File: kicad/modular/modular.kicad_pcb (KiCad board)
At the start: 2 copper layers, 119.1 x 78 mm, 84 parts, among them J1 CONN_PWR, J2 HEADER, J3 HEADER, J4 Header, J5 DIFFX, J6 DIFFY, J7 SUM, U1 LM317, U2 LM337, U3 REF5010, U4 OPA4197, U5 OPA197, U6 OPA2197

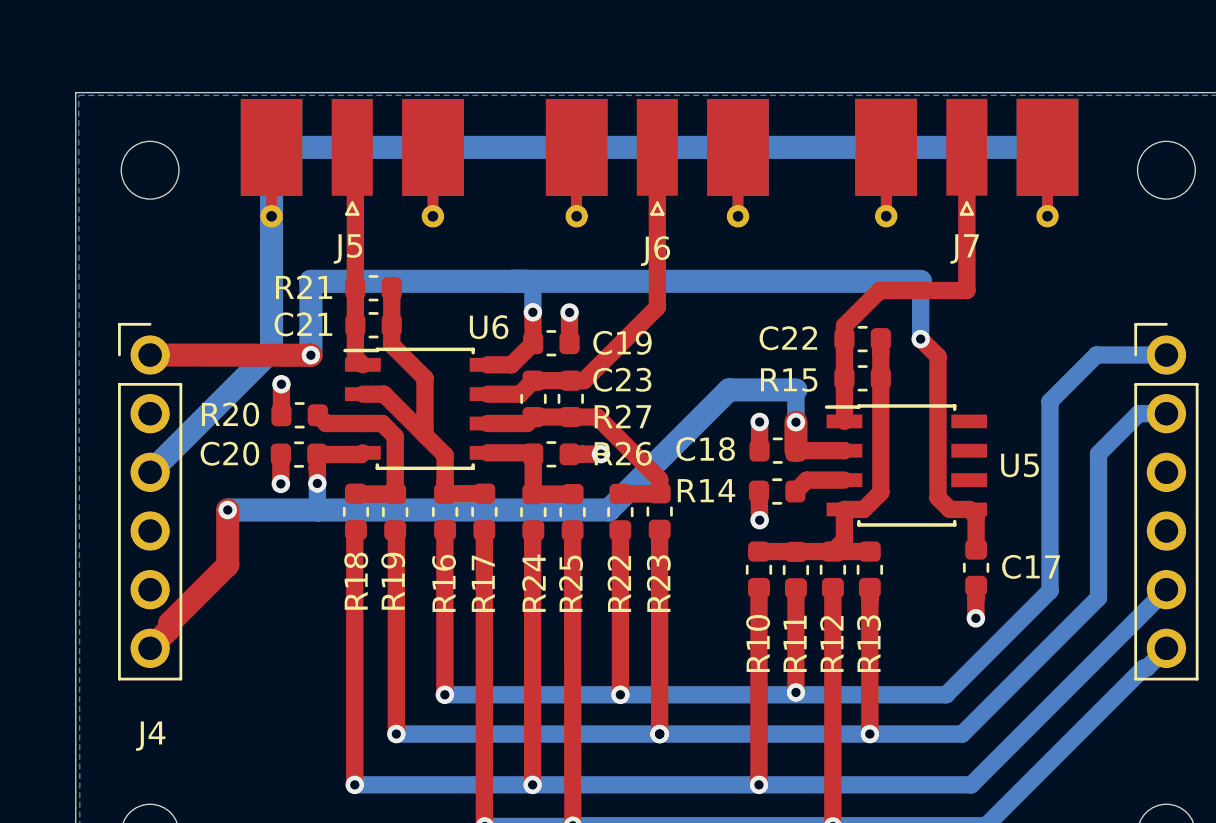
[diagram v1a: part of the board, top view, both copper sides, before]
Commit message: fixed generic opamp symbol pin layout, updated pcb of arithmetic board
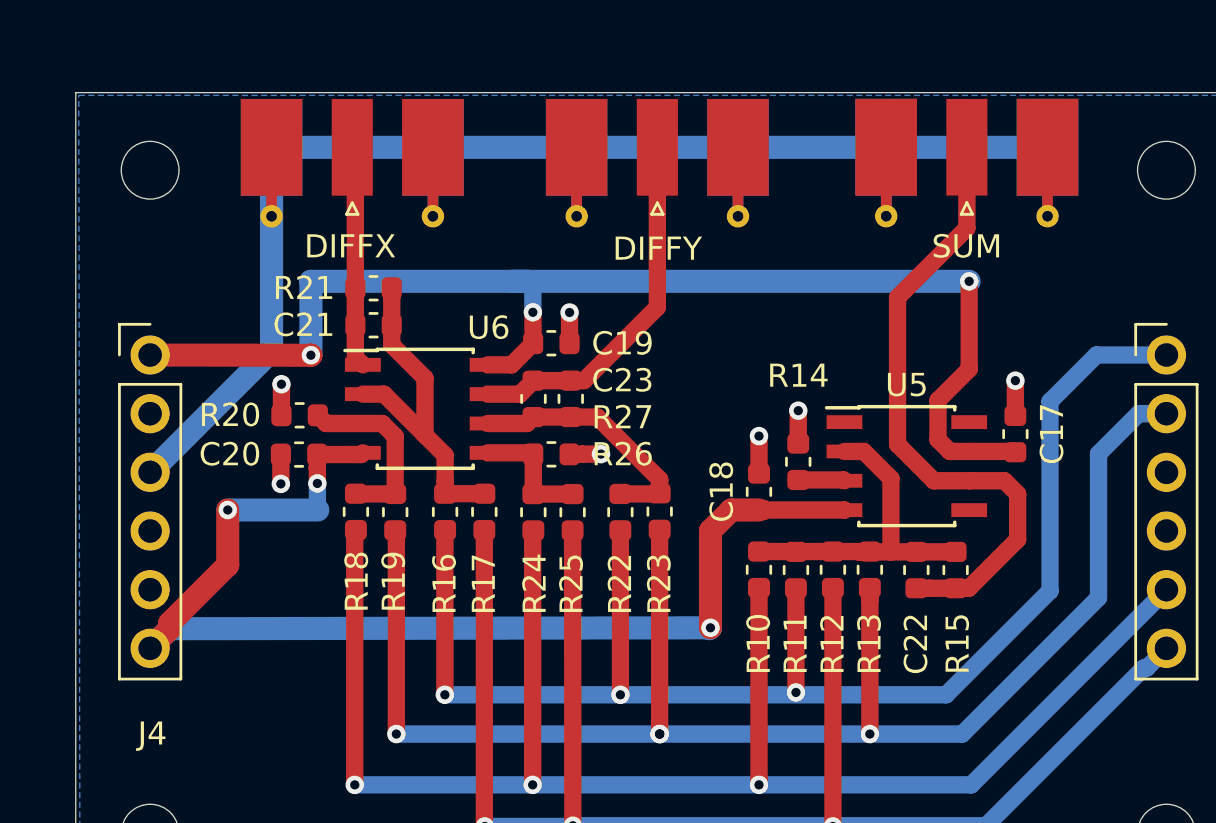
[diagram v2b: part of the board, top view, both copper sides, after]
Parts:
- moved C22 10.3 mm to (199.5, 106.8), turned to 90 degrees
- moved R15 9.22 mm to (201.2, 106.8), turned to 90 degrees
- moved C17 6.03 mm to (203.8, 100.9), turned to 90 degrees
- moved C18 1.96 mm to (192.7, 103.4), turned to 90 degrees
- moved R14 1.58 mm to (194.4, 102.1), turned to 270 degrees
- renumbered J5 to DIFFX, J6 to DIFFY, J7 to SUM
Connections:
- U5 pad 1: /Arithmetic/SUM -> (no net)
- U5 pad 2: -12V -> Net-(C22-Pad2)
- U5 pad 4: Net-(C22-Pad2) -> -12V
- U5 pad 5: +12V -> (no net)
- U5 pad 6: (no net) -> /Arithmetic/SUM
- U5 pad 7: (no net) -> +12V
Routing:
- net /Arithmetic/SUM: track 16.3 -> 27.4 mm
- net -12V: track 151.1 -> 158.5 mm
- net Net-(C22-Pad2): track 15.4 -> 14.7 mm
- net GND: track 310.1 -> 310.7 mm
